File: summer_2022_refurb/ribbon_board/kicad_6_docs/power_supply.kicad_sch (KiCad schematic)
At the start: 4 parts

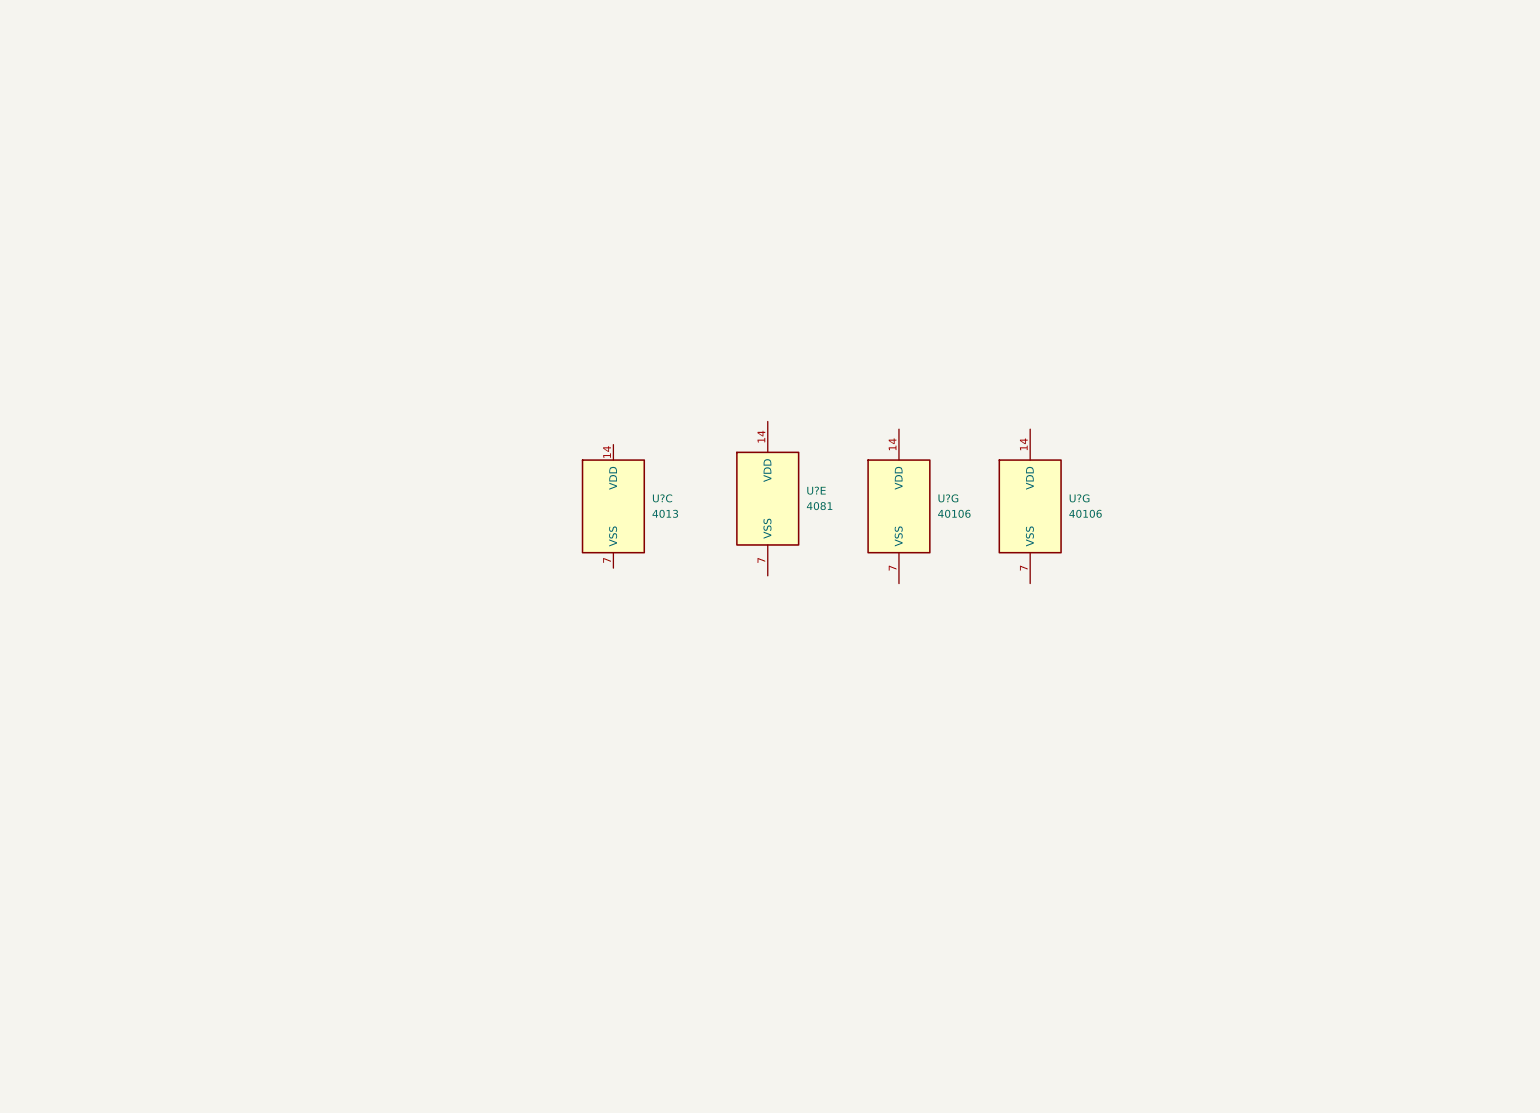
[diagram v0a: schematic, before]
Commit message: Progress on ribbon board
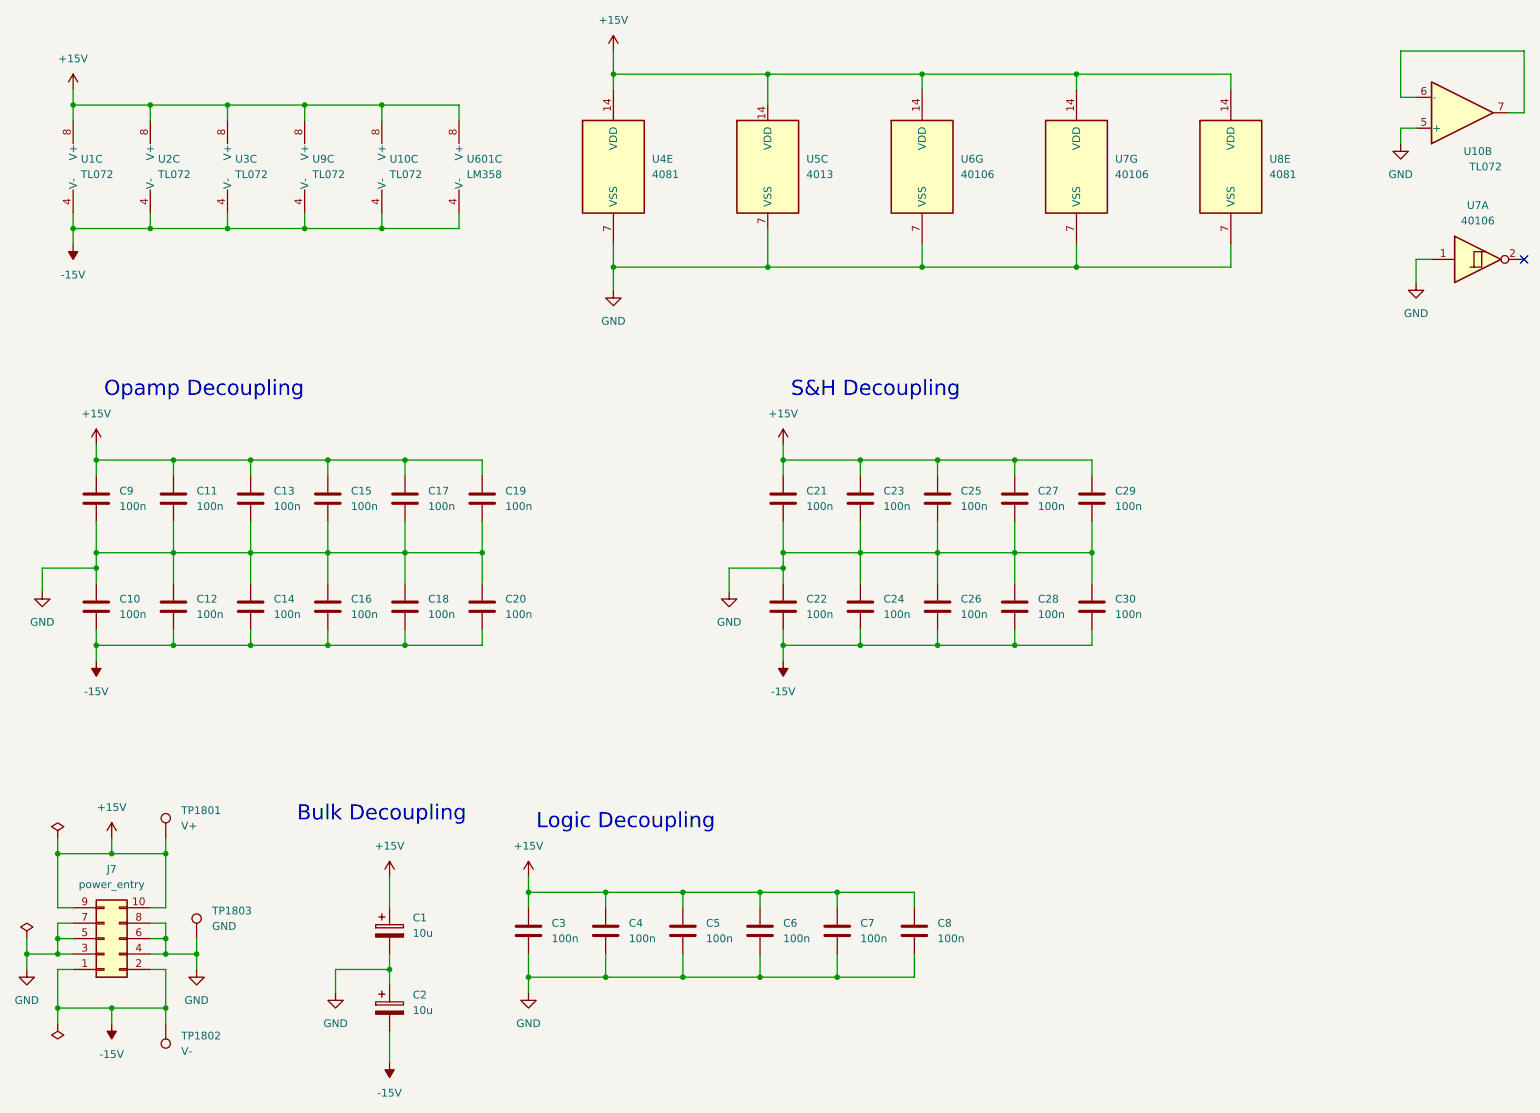
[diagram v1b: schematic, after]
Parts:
- added C1, C2: 10u, Capacitor_THT:CP_Radial_D6.3mm_P2.50mm, symbol Device:C_Polarized
- added C10, C11, C12, C13, C14, C15, C16, C17, C18, C19, C20, C21, C22, C23, C24, C25, C26, C27, C28, C29, C3, C30, C4, C5, C6, C7, C8, C9: 100n, Capacitor_SMD:C_0805_2012Metric, symbol Device:C
- added J7: power_entry, Connector_IDC:IDC-Header_2x05_P2.54mm_Vertical, symbol Connector_Generic:Conn_02x05_Odd_Even
- added TP1801: V+, TestPoint:TestPoint_Keystone_5000-5004_Miniature, symbol Connector:TestPoint
- added TP1802: V-, TestPoint:TestPoint_Keystone_5000-5004_Miniature, symbol Connector:TestPoint
- added TP1803: GND, TestPoint:TestPoint_Bridge_Pitch7.62mm_Drill1.3mm, symbol Connector:TestPoint
- added U1, U10, U2, U3, U9: TL072, Package_SO:SO-8_5.3x6.2mm_P1.27mm, symbol Amplifier_Operational:TL072
- added U601: LM358, Package_SO:SOIC-8_3.9x4.9mm_P1.27mm, symbol Amplifier_Operational:LM358
- added unit 1 of U7
- added U8: 4081, Package_SO:SOIC-14_3.9x8.7mm_P1.27mm, symbol 4xxx:4081
- U4, U5, U6, U7: renamed from U?; footprint (none) -> Package_SO:SOIC-14_3.9x8.7mm_P1.27mm
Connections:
- net +15V: now reaches U7.14 (VDD)
- net +15V: now also U4.14 (VDD), U5.14 (VDD), U6.14 (VDD), C1.1, C11.1, C13.1, C15.1, C17.1, C19.1, C21.1, C23.1, C25.1, C27.1, C29.1, C3.1, C4.1, C5.1, C6.1, C7.1, C8.1, C9.1, J7.10 (Pin_10), J7.9 (Pin_9), TP1801.1, U1.8 (V+), U10.8 (V+), U2.8 (V+), U3.8 (V+), U601.8 (V+), U8.14 (VDD), U9.8 (V+)
- net GND: now reaches U7.7 (VSS)
- net GND: now also U4.7 (VSS), U5.7 (VSS), U6.7 (VSS), C1.2, C10.1, C11.2, C12.1, C13.2, C14.1, C15.2, C16.1, C17.2, C18.1, C19.2, C2.1, C20.1, C21.2, C22.1, C23.2, C24.1, C25.2, C26.1, C27.2, C28.1, C29.2, C3.2, C30.1, C4.2, C5.2, C6.2, C7.2, C8.2, C9.2, J7.3 (Pin_3), J7.4 (Pin_4), J7.5 (Pin_5), J7.6 (Pin_6), J7.7 (Pin_7), J7.8 (Pin_8), TP1803.1, U10.5 (+), U7.1, U8.7 (VSS)
- new net: U10.6 (-), U10.7
- new net -15V: C10.2, C12.2, C14.2, C16.2, C18.2, C2.2, C20.2, C22.2, C24.2, C26.2, C28.2, C30.2, J7.1 (Pin_1), J7.2 (Pin_2), TP1802.1, U1.4 (V-), U10.4 (V-), U2.4 (V-), U3.4 (V-), U601.4 (V-), U9.4 (V-)
- no-connect marks 0 -> 1
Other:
- note added: "Bulk Decoupling"
- note added: "Logic Decoupling"
- note added: "Opamp Decoupling"
- note added: "S&H Decoupling"
- moved on the sheet: U4E, U5C, U6G, U7G
